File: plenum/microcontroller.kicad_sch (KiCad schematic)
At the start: 19 parts, among them J1 Conn_02x01, J2 Conn_02x08_Odd_Even, U1 PIC18F66J60-IPT, Y1 25 MHz

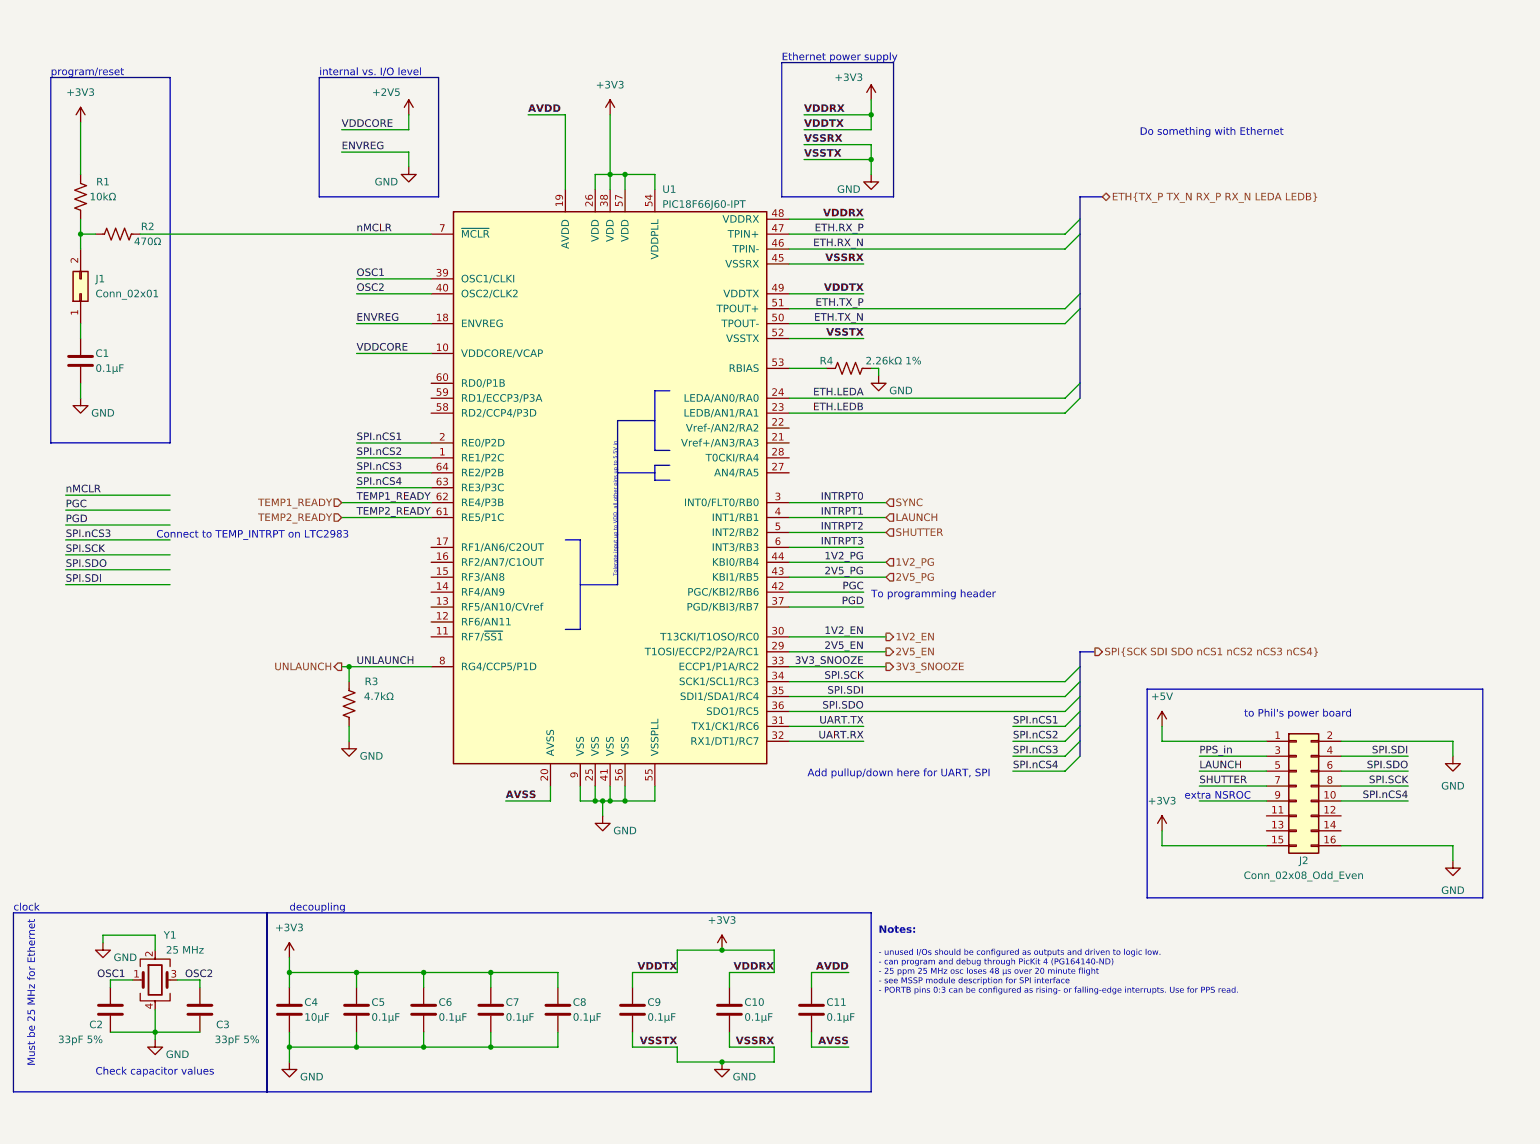
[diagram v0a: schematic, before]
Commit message: adding housekeeping board
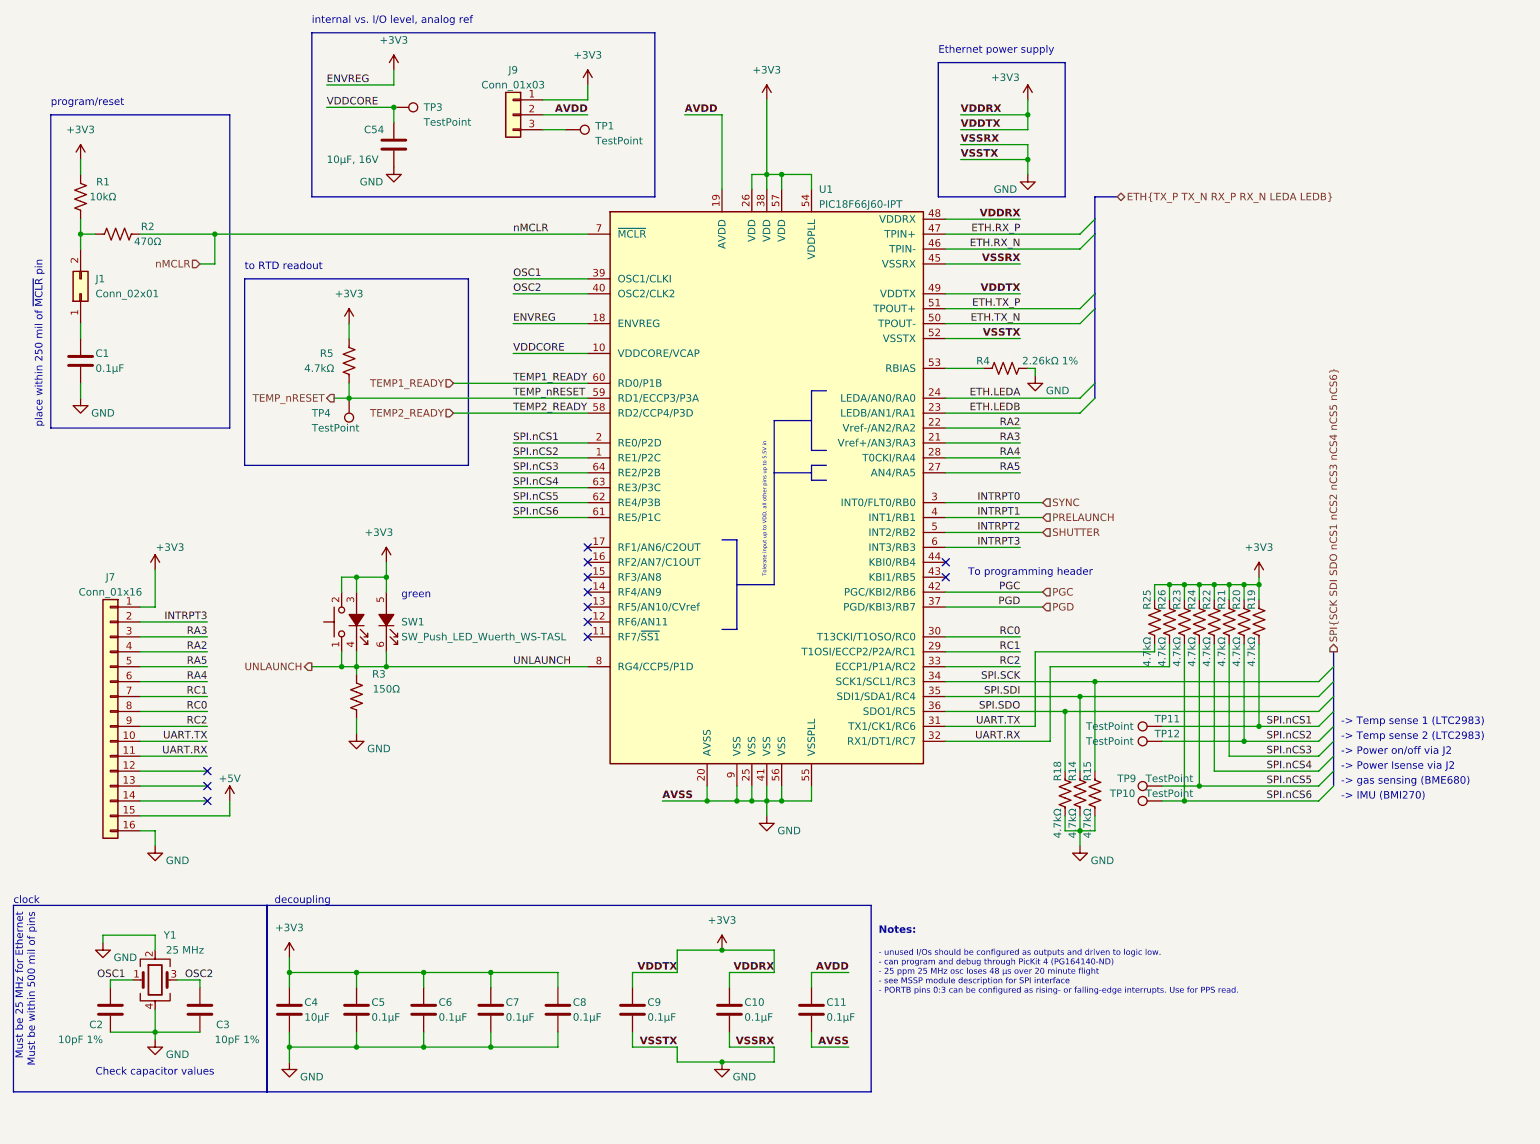
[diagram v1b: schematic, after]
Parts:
- removed J2: Conn_02x08_Odd_Even, symbol Connector_Generic:Conn_02x08_Odd_Even
- added C54: 10µF, 16V, Capacitor_SMD:C_0603_1608Metric, symbol Device:C
- added J7: Conn_01x16, Connector_PinHeader_2.54mm:PinHeader_1x16_P2.54mm_Vertical, symbol Connector_Generic:Conn_01x16
- added J9: Conn_01x03, Connector_PinSocket_2.54mm:PinSocket_1x03_P2.54mm_Vertical, symbol Connector_Generic:Conn_01x03
- added R14, R15, R18, R19, R20, R21, R22, R23, R24, R25, R26, R5: 4.7kΩ, Resistor_SMD:R_0603_1608Metric, symbol Device:R_US
- added SW1: SW_Push_LED_Wuerth_WS-TASL, Button_Switch_SMD:SW_Tactile_SPST_Wuerth_WS-TASL, symbol Switch:SW_Push_LED_Wuerth_WS-TASL
- added TP1: TestPoint, TestPoint:TestPoint_Loop_D2.60mm_Drill1.4mm_Beaded, symbol Connector:TestPoint
- added TP10, TP11, TP12, TP4, TP9: TestPoint, TestPoint:TestPoint_THTPad_D2.0mm_Drill1.0mm, symbol Connector:TestPoint
- added TP3: TestPoint, TestPoint:TestPoint_Pad_1.5x1.5mm, symbol Connector:TestPoint
- C1, C10, C11, C5, C6, C7, C8, C9: footprint Capacitor_SMD:C_0402_1005Metric -> Capacitor_SMD:C_0603_1608Metric
- C2, C3: value 33pF 5% -> 10pF 1%
- J1: footprint Connector_PinHeader_1.27mm:PinHeader_1x02_P1.27mm_Vertical -> Connector_PinHeader_2.54mm:PinHeader_1x02_P2.54mm_Vertical
- R3: value 4.7kΩ -> 150Ω
- U1: Digikey (none) -> PIC18F66J60-I/PT-ND
- Y1: footprint (none) -> Crystal:Crystal_SMD_3225-4Pin_3.2x2.5mm; Digikey (none) -> XC2480CT-ND
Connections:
- net AVSS is gone; now on net GND: C11.2, U1.20 (AVSS)
- net +3V3: now also U1.18 (ENVREG), J7.1 (Pin_1), J9.1 (Pin_1), R19.2, R20.2, R21.2, R22.2, R23.2, R24.2, R25.2, R26.2, R5.2, SW1.2 (sw2), SW1.3 (A), SW1.5 (A)
- net +5V: now also J7.15 (Pin_15)
- net AVDD: now also J9.2 (Pin_2)
- net GND: now also C54.2, J7.16 (Pin_16), R14.1, R15.1, R18.1; no longer U1.18 (ENVREG)
- net INTRPT3: now also J7.2 (Pin_2)
- net SPI.SCK: now also R15.2
- net SPI.SDI: now also R14.2
- net SPI.SDO: now also R18.2
- net SPI.nCS1: now also R19.1, TP11.1
- net SPI.nCS2: now also R20.1, TP12.1
- net SPI.nCS3: now also R21.1
- net SPI.nCS4: now also R22.1
- net TEMP1_READY: now also U1.60 (RD0/P1B); no longer U1.62 (RE4/P3B)
- net TEMP2_READY: now also U1.58 (RD2/CCP4/P3D); no longer U1.61 (RE5/P1C)
- net UART.RX: now also J7.11 (Pin_11), R26.1
- net UART.TX: now also J7.10 (Pin_10), R25.1
- net UNLAUNCH: now also SW1.1 (sw1), SW1.4 (K), SW1.6 (K)
- net RA3: now reaches U1.21 (Vref+/AN3/RA3)
- net RA3: now also J7.3 (Pin_3)
- net RA2: now reaches U1.22 (Vref-/AN2/RA2)
- net RA2: now also J7.4 (Pin_4)
- net RA5: now reaches U1.27 (AN4/RA5)
- net RA5: now also J7.5 (Pin_5)
- net RA4: now reaches U1.28 (T0CKI/RA4)
- net RA4: now also J7.6 (Pin_6)
- net TEMP_nRESET: now reaches U1.59 (RD1/ECCP3/P3A)
- net TEMP_nRESET: now also R5.1, TP4.1
- net +2V5 renamed VDDCORE
- net VDDCORE: now also C54.1, TP3.1
- net 1V2_EN renamed RC0
- net RC0: now also J7.8 (Pin_8)
- net 1V2_PG: no longer names the net of U1.44 (KBI0/RB4)
- net 2V5_EN renamed RC1
- net RC1: now also J7.7 (Pin_7)
- net 2V5_PG: no longer names the net of U1.43 (KBI1/RB5)
- net 3V3_SNOOZE renamed RC2
- net RC2: now also J7.9 (Pin_9)
- net LAUNCH renamed PRELAUNCH
- new net: J9.3 (Pin_3), TP1.1
- new net SPI.nCS5: R24.1, TP9.1, U1.62 (RE4/P3B)
- new net SPI.nCS6: R23.1, TP10.1, U1.61 (RE5/P1C)
- no-connect marks 0 -> 12
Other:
- note added: "-> IMU (BMI270)"
- note added: "-> Power Isense via J2"
- note added: "-> Power on/off via J2"
- note added: "-> Temp sense 1 (LTC2983)"
- note added: "-> Temp sense 2 (LTC2983)"
- note added: "-> gas sensing (BME680)"
- note added: "Must be 25 MHz for Ethernet Must be within 500 mil of pins"
- note added: "green"
- note added: "internal vs. I/O level, analog ref"
- note added: "place within 250 mil of ~{MCLR} pin"
- note added: "to RTD readout"
- note removed: "Add pullup/down here for UART, SPI"
- note removed: "Connect to TEMP_INTRPT on LTC2983"
- note removed: "Do something with Ethernet"
- note removed: "Must be 25 MHz for Ethernet"
- note removed: "extra NSROC"
- note removed: "internal vs. I/O level"
- note removed: "to Phil's power board"
- moved on the sheet: R3, R4, U1
